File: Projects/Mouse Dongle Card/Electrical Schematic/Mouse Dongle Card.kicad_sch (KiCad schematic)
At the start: 11 parts, among them J1 692121330100, P1 USB_C_Plug

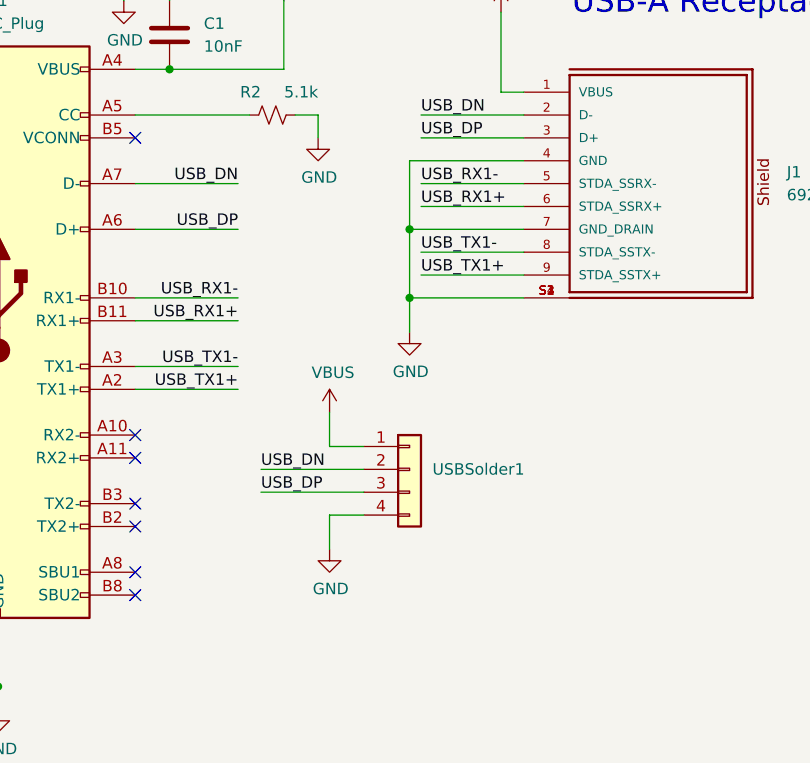
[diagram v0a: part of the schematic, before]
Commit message: Preliminary layout of mag card
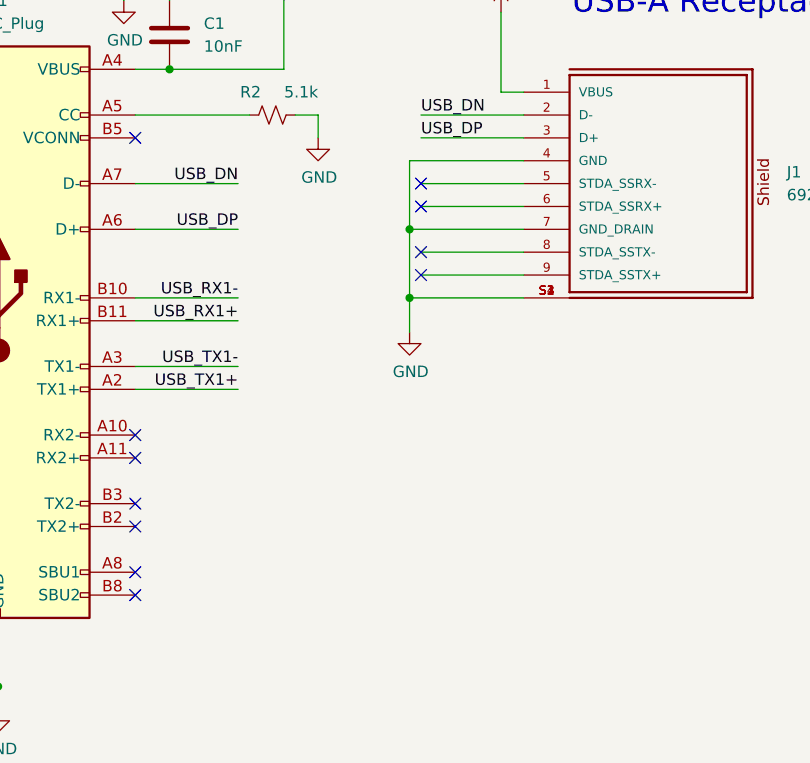
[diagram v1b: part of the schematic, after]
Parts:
- removed USBSolder1: ~, USB_A_PCB_Edge_receptacle, symbol Connector_Generic:Conn_01x04
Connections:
- net USB_RX1+: no longer J1.6 (STDA_SSRX+)
- net USB_RX1-: no longer J1.5 (STDA_SSRX-)
- net USB_TX1+: no longer J1.9 (STDA_SSTX+)
- net USB_TX1-: no longer J1.8 (STDA_SSTX-)
- no-connect marks 7 -> 11
